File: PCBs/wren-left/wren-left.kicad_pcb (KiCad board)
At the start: 2 copper layers, 230.3 x 117 mm, 102 parts, among them J1 TRRS_Jack, SW0 Reset, U1 Elite-C

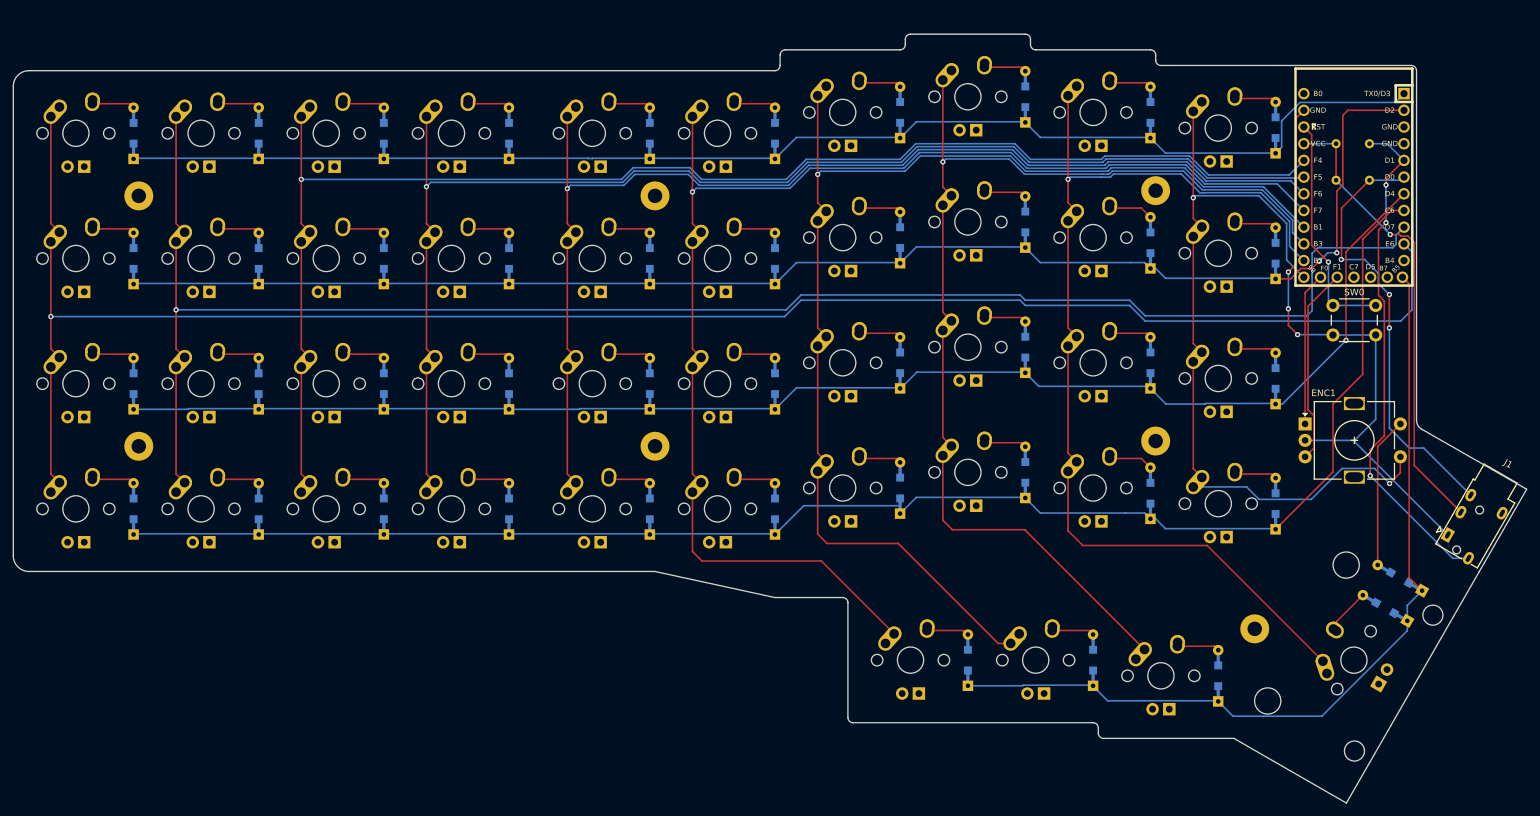
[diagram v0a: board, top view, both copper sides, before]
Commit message: Reposition Rotary Encoder and Create New Right Board
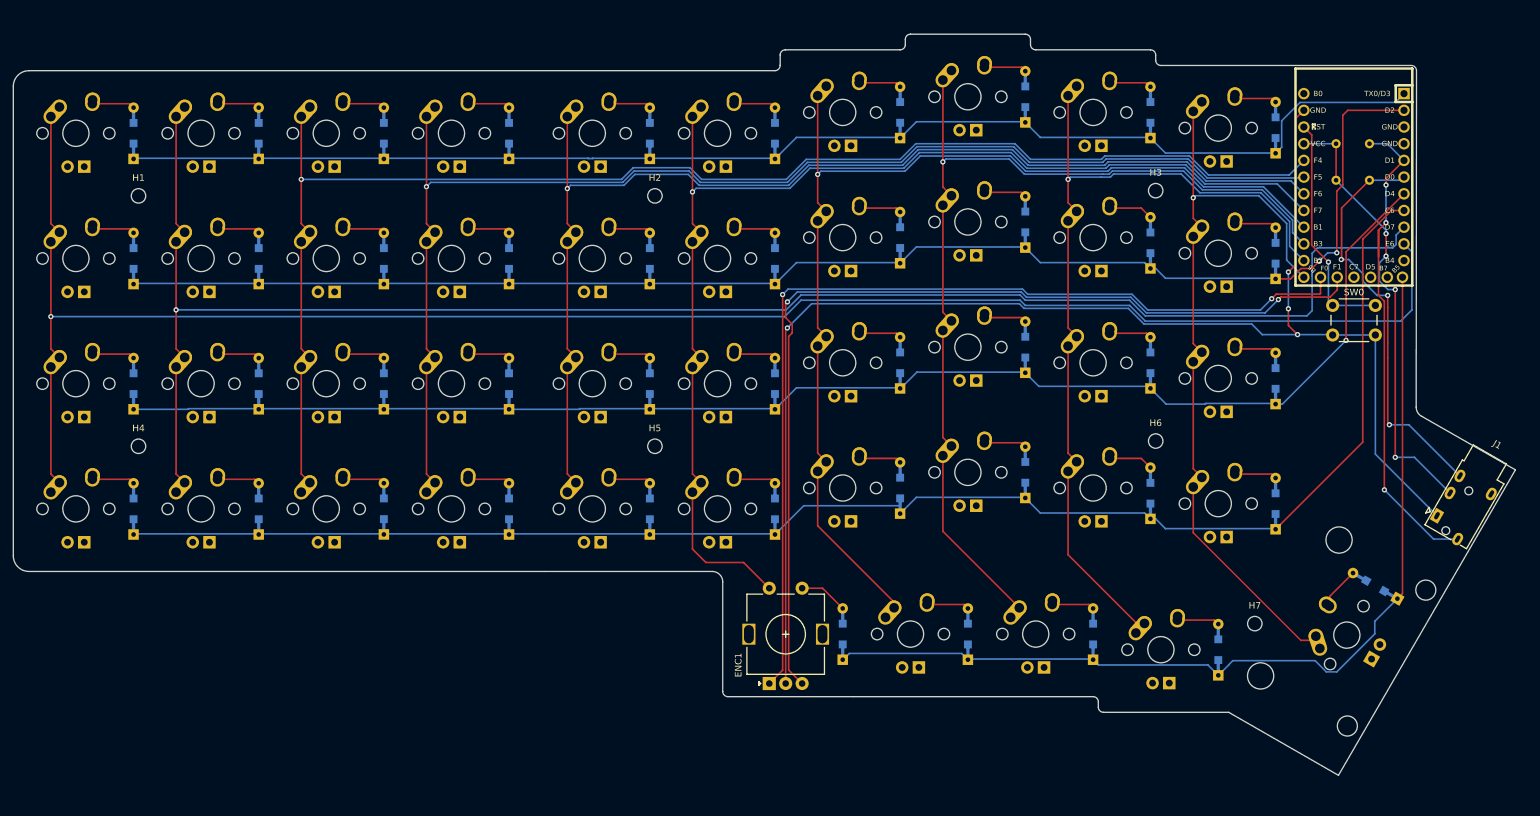
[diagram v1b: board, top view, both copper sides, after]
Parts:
- removed REF** (x7): MountingHole_2.2mm_M2_Pad, MountingHole:MountingHole_2.2mm_M2_Pad
- added H1: MountingHole, MountingHole:MountingHole_2.2mm_M2_ISO7380, F.Cu at (56.4, 46.0)
- added H2: MountingHole, MountingHole:MountingHole_2.2mm_M2_ISO7380, F.Cu at (134.9, 46.0)
- added H3: MountingHole, MountingHole:MountingHole_2.2mm_M2_ISO7380, F.Cu at (211.1, 45.2)
- added H4: MountingHole, MountingHole:MountingHole_2.2mm_M2_ISO7380, F.Cu at (56.4, 84.1)
- added H5: MountingHole, MountingHole:MountingHole_2.2mm_M2_ISO7380, F.Cu at (134.9, 84.1)
- added H6: MountingHole, MountingHole:MountingHole_2.2mm_M2_ISO7380, F.Cu at (211.1, 83.3)
- added H7: MountingHole, MountingHole:MountingHole_2.2mm_M2_ISO7380, F.Cu at (226.2, 111.1)
- moved ENC1 90.6 mm to (152.3, 120.2), turned to 90 degrees
- moved D42 26.2 mm to (220.7, 115.1), turned to 90 degrees
- moved D43 20.1 mm to (201.6, 112.7)
- moved D45 19.5 mm to (163.5, 112.7)
- moved D44 19.5 mm to (182.6, 112.7)
- moved MX42 3.97 mm to (211.9, 115.1)
- moved MX43 3.97 mm to (192.9, 112.7)
- moved MX44 3.97 mm to (173.8, 112.7)
- moved MX41 3.96 mm to (240.2, 112.9)
- moved D41 3.95 mm to (244.5, 105.4)
- moved J1 3.36 mm to (253.9, 94.7)
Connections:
- D41 pad 2: ENC1-OUT -> Net-(D41-Pad2)
- D45 pad 2: Net-(D45-Pad2) -> ENC1-IN
- ENC1 pad S1: COL0 -> ENC1-IN
- ENC1 pad S2: ENC1-OUT -> COL4
- MX41 pad 1: COL1 -> COL0
- MX41 pad 2: Net-(D42-Pad2) -> Net-(D41-Pad2)
- MX42 pad 1: COL2 -> COL1
- MX42 pad 2: Net-(D43-Pad2) -> Net-(D42-Pad2)
- MX43 pad 1: COL3 -> COL2
- MX43 pad 2: Net-(D44-Pad2) -> Net-(D43-Pad2)
- MX44 pad 1: COL4 -> COL3
- MX44 pad 2: Net-(D45-Pad2) -> Net-(D44-Pad2)
- U1 pad 11: (no net) -> Net-(U1-Pad11)
- U1 pad 24: (no net) -> Net-(U1-Pad24)
- U1 pad 25: (no net) -> Net-(U1-Pad25)
- U1 pad 26: (no net) -> Net-(U1-Pad26)
- U1 pad 27: (no net) -> Net-(U1-Pad27)
- U1 pad 3: (no net) -> Net-(U1-Pad3)
- U1 pad 4: (no net) -> Net-(U1-Pad4)
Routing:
- net LEFT: track 23.3 -> 147.0 mm, vias 0 -> 2
- net GND: track 92.8 -> 214.3 mm, vias 3 -> 4
- net RIGHT: track 30.1 -> 148.6 mm, vias 0 -> 2
- net COL1: track 154.3 -> 127.4 mm
- net ENC1-OUT: track 22.9 -> 0.00 mm
- net COL4: track 198.9 -> 176.8 mm
- net COL2: track 165.0 -> 144.3 mm
- net COL3: track 180.2 -> 160.0 mm
- net ROW4: track 130.2 -> 142.9 mm
- net ENC1-IN: track 0.00 -> 7.45 mm
- net Net-(D41-Pad2): track 0.00 -> 6.51 mm
- net Net-(D45-Pad2): track 6.48 -> 0.00 mm
- net COL0: track 118.0 -> 113.2 mm, vias 2 -> 1
- net SCL: track 66.7 -> 63.1 mm
- net VCC: track 70.3 -> 68.4 mm, vias 1 -> 4
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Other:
- board size 230.3 x 117 mm -> 228.6 x 112.8 mm

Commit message: Various Updates
New plates, updated routing on the right side, assorted other changes.
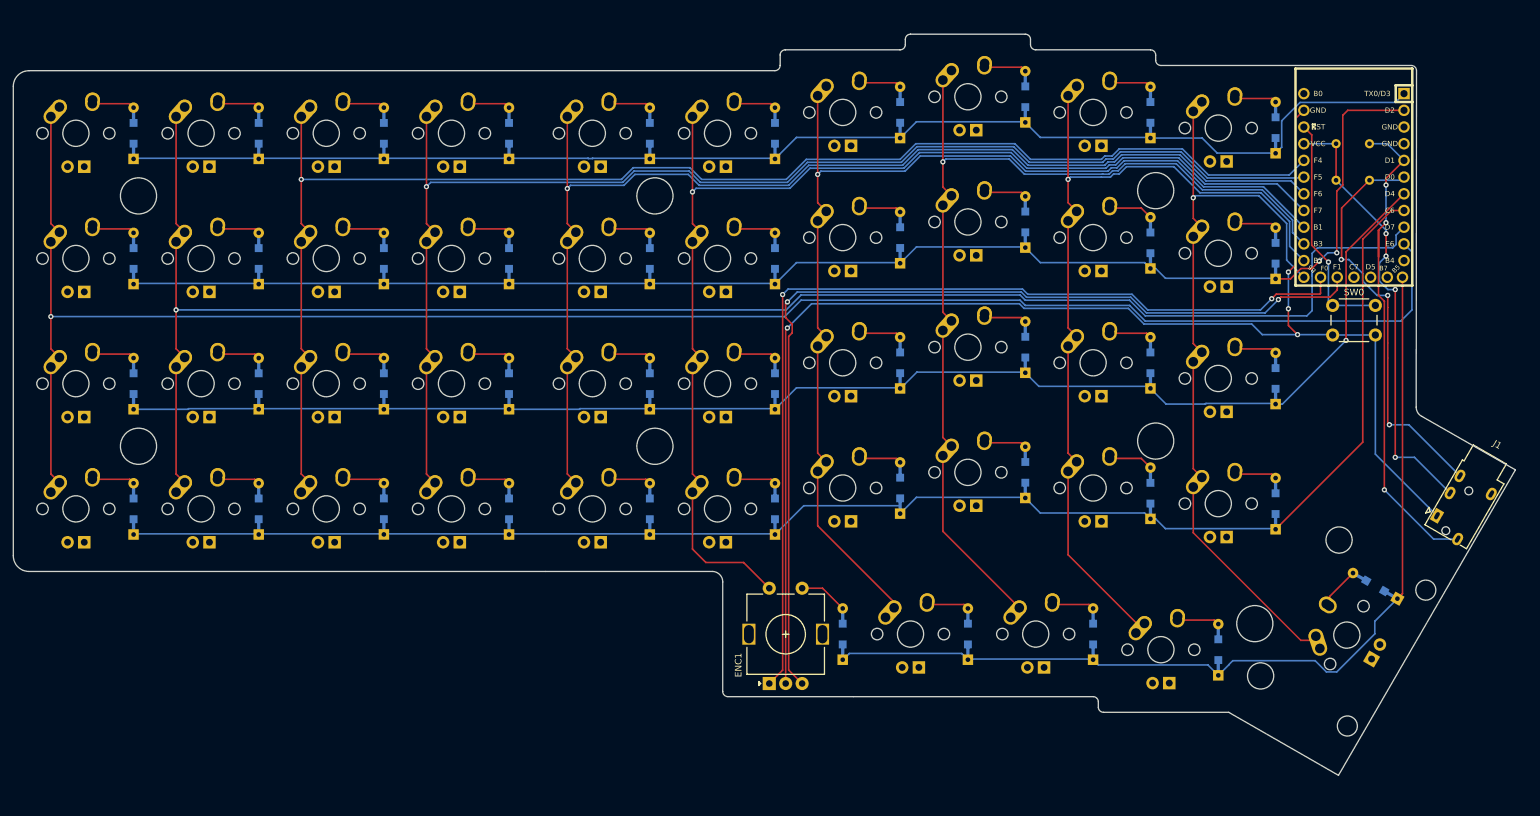
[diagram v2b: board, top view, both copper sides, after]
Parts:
- H1, H2, H3, H4, H5, H6, H7: footprint MountingHole:MountingHole_2.2mm_M2_ISO7380 -> MountingHole:MountingHole_5.5mm
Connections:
- U1 pad 11: Net-(U1-Pad11) -> (no net)
- U1 pad 24: Net-(U1-Pad24) -> (no net)
- U1 pad 25: Net-(U1-Pad25) -> (no net)
- U1 pad 26: Net-(U1-Pad26) -> (no net)
- U1 pad 27: Net-(U1-Pad27) -> (no net)
- U1 pad 3: Net-(U1-Pad3) -> (no net)
- U1 pad 4: Net-(U1-Pad4) -> (no net)
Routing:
- net COL2: track 144.3 -> 145.3 mm
- net COL1: track 127.4 -> 128.4 mm
- net COL7: track 214.0 -> 214.9 mm
- net COL6: track 194.5 -> 195.4 mm
- net COL5: track 173.5 -> 174.4 mm
- net COL3: track 160.0 -> 160.9 mm
- net COL4: track 176.8 -> 177.7 mm

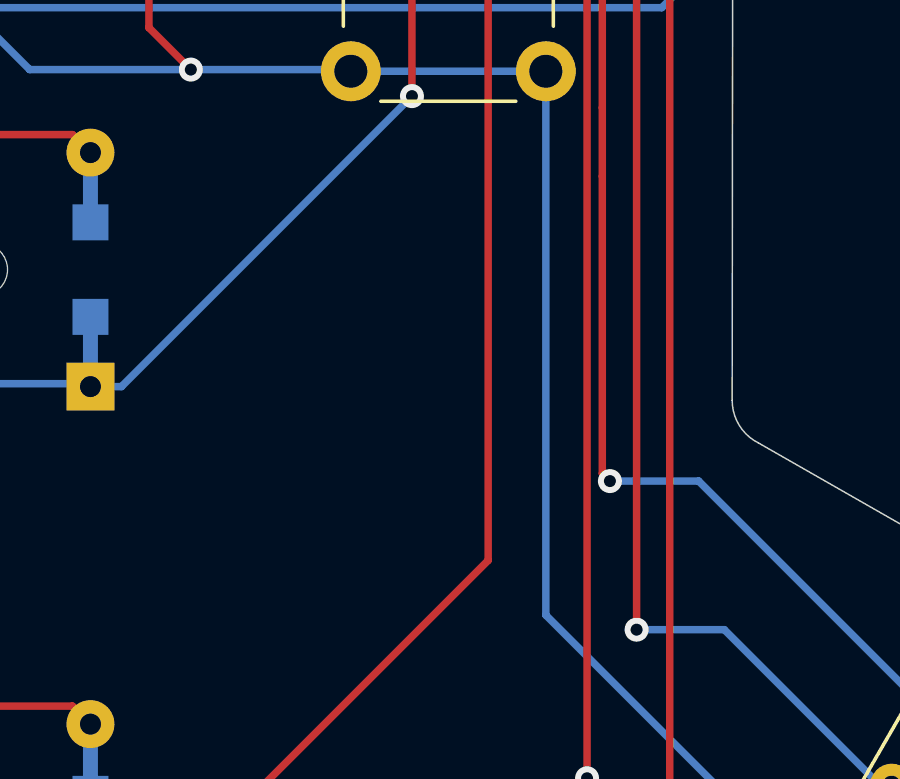
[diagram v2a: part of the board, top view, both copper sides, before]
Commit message: Add Wren Logo (Pt. 2)
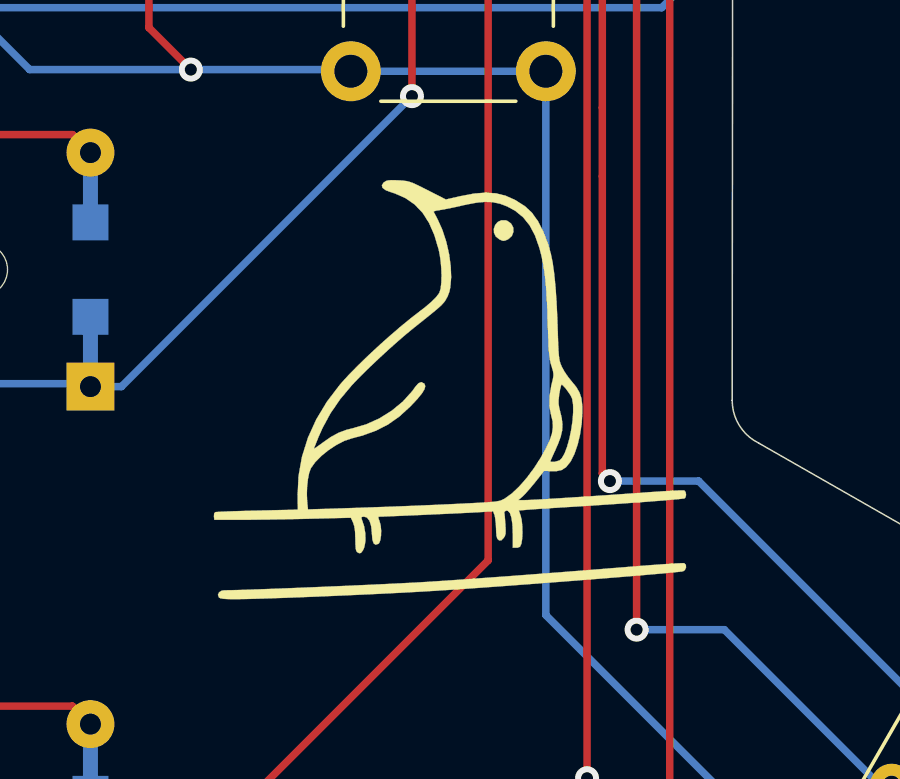
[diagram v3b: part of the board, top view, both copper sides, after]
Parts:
- added G***: LOGO, footprints:wren_logo, F.Cu at (241.4, 77.8)

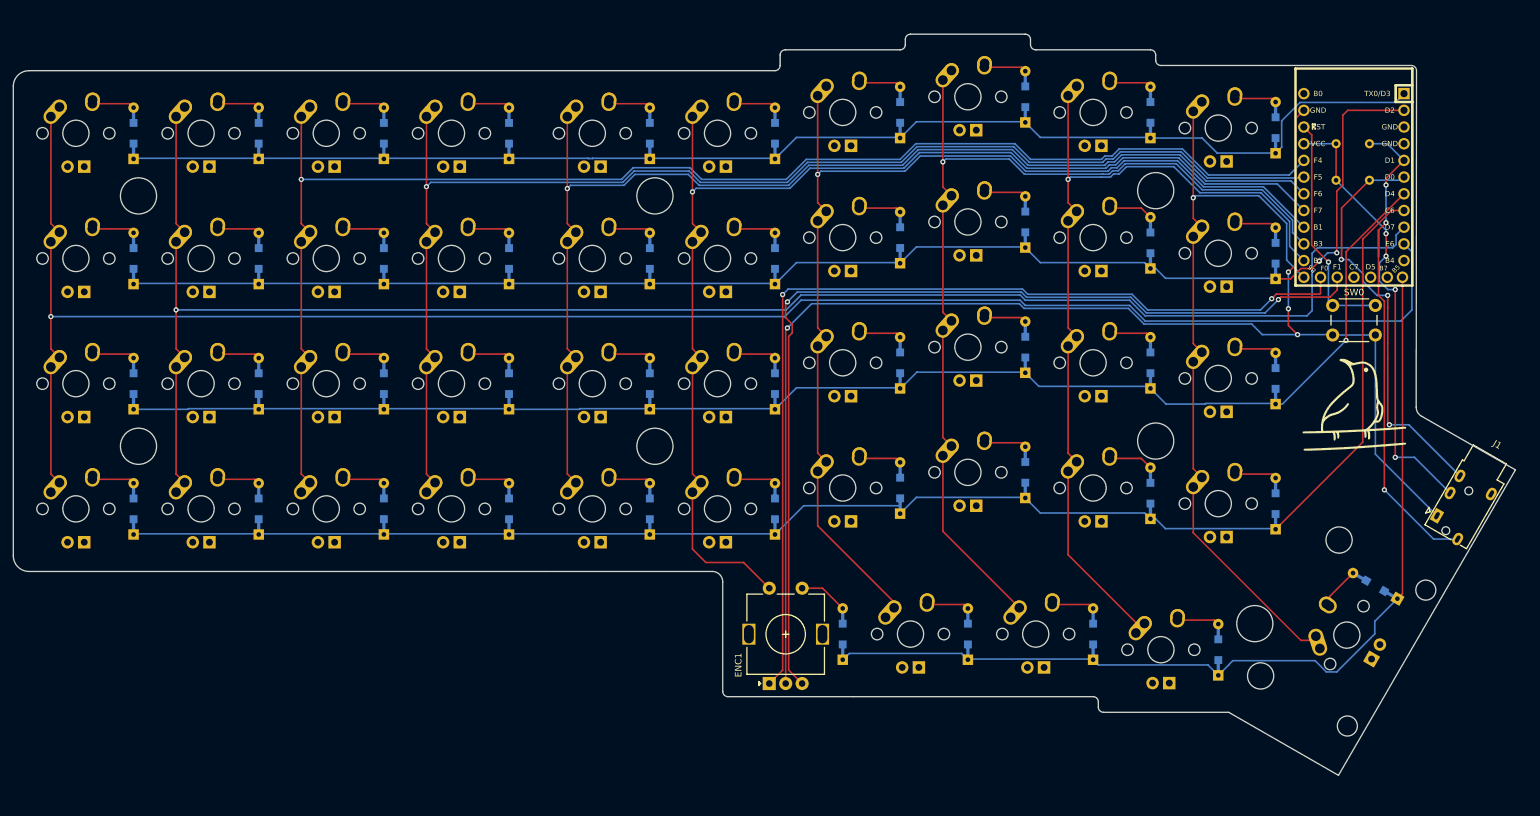
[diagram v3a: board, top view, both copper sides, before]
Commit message: Use insight on rotary encoder position to adopt more Kyria-like stagger
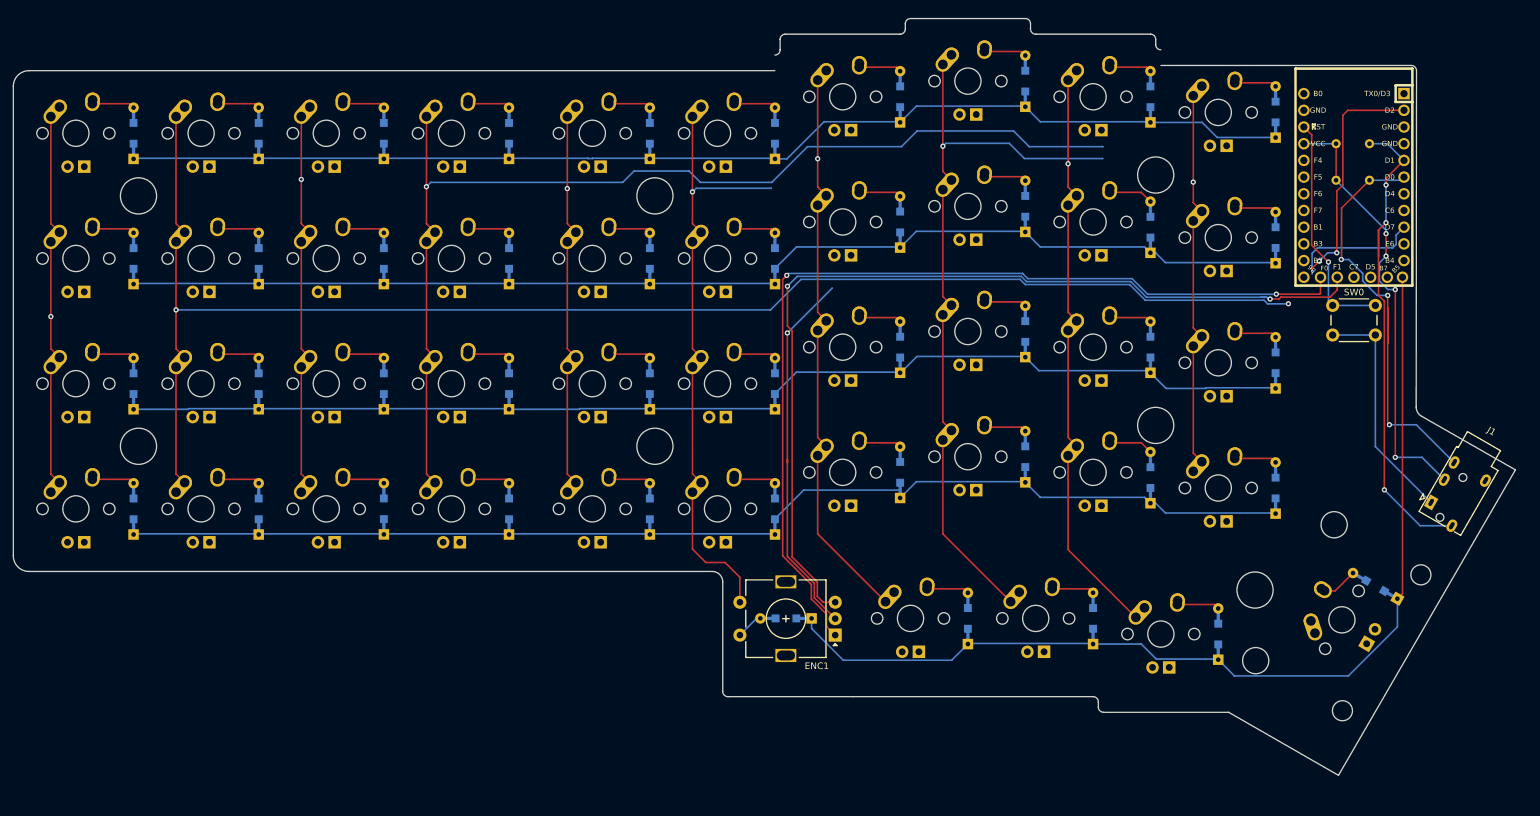
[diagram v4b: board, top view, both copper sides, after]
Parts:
- removed G***: LOGO, footprints:wren_logo
- moved ENC1 12.4 mm to (162.4, 112.9), turned to 180 degrees
- moved D45 8.96 mm to (154.9, 110.3), turned to 180 degrees
- moved H7 5.11 mm to (226.3, 106.0)
- moved MX41 2.44 mm to (239.5, 110.5)
- moved D42 2.38 mm to (220.7, 112.7)
- moved MX42 2.38 mm to (211.9, 112.7)
- moved D43 2.38 mm to (201.6, 110.3)
- moved D23 2.38 mm to (191.3, 66.7)
- moved D31 2.38 mm to (229.4, 90.5)
- moved D33 2.38 mm to (191.3, 85.7)
- moved D44 2.38 mm to (182.6, 110.3)
- moved MX23 2.38 mm to (182.6, 66.7)
- moved MX31 2.38 mm to (220.7, 90.5)
- moved MX33 2.38 mm to (182.6, 85.7)
- moved MX43 2.38 mm to (192.9, 110.3)
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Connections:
- ENC1 pad S1: ENC1-IN -> COL4
- ENC1 pad S2: COL4 -> ENC1-IN
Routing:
- net COL9: track 275.1 -> 54.4 mm
- net COL7: track 214.9 -> 54.4 mm
- net GND: track 214.3 -> 92.1 mm, vias 4 -> 1
- net COL5: track 174.4 -> 54.4 mm
- net COL4: track 177.7 -> 88.1 mm
- net COL3: track 160.9 -> 80.9 mm
- net COL0: track 113.2 -> 54.4 mm
- net ROW3: track 236.9 -> 179.2 mm
- net COL1: track 128.4 -> 83.3 mm
- net ROW2: track 219.2 -> 178.5 mm, vias 1 -> 0
- net COL2: track 145.3 -> 108.7 mm
- net COL6: track 195.4 -> 163.6 mm
- net ROW0: track 203.9 -> 179.3 mm
- net ROW4: track 142.9 -> 152.4 mm
- net COL8: track 255.3 -> 246.7 mm, vias 1 -> 2
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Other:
- board size 228.6 x 112.8 mm -> 228.6 x 115.2 mm
